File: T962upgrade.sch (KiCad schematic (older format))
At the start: 1 part

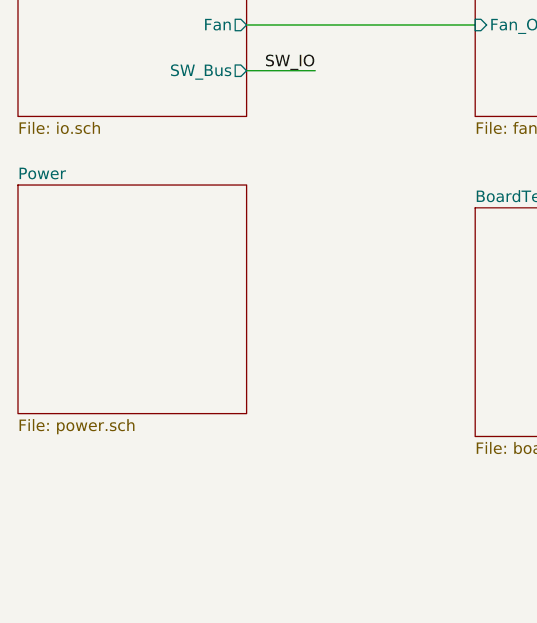
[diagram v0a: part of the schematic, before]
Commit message: Added optional through hole resistor to set fan switch on temperature.
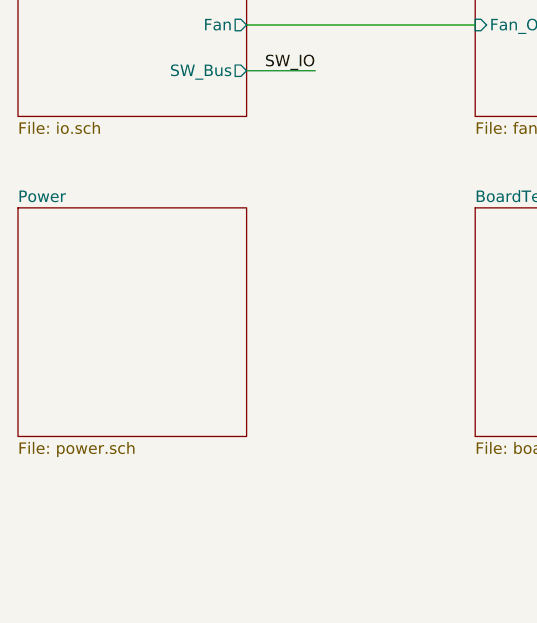
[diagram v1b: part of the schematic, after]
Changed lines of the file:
@@
 $EndSheet
 $Sheet
-S 4000 3900 1000 1000
+S 4000 4000 1000 1000
 U 5E3D0FD8
 F0 "Power" 50
